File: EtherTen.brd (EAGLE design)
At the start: 68.6 x 53.3 mm, 103 parts, among them IC1 MC33269DT-5.0, IC2 APX811-44UG-7, IC3 ATMEGA16U2-MU, IC4 LM358D, IC5 ATMEGA328P TQFP32, IC6 W5100SQFP80, IC7 MCP24AA025E48, J1 DC_2_1MM, P1 USB-6PSMT, P2 ICSP:MAIN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

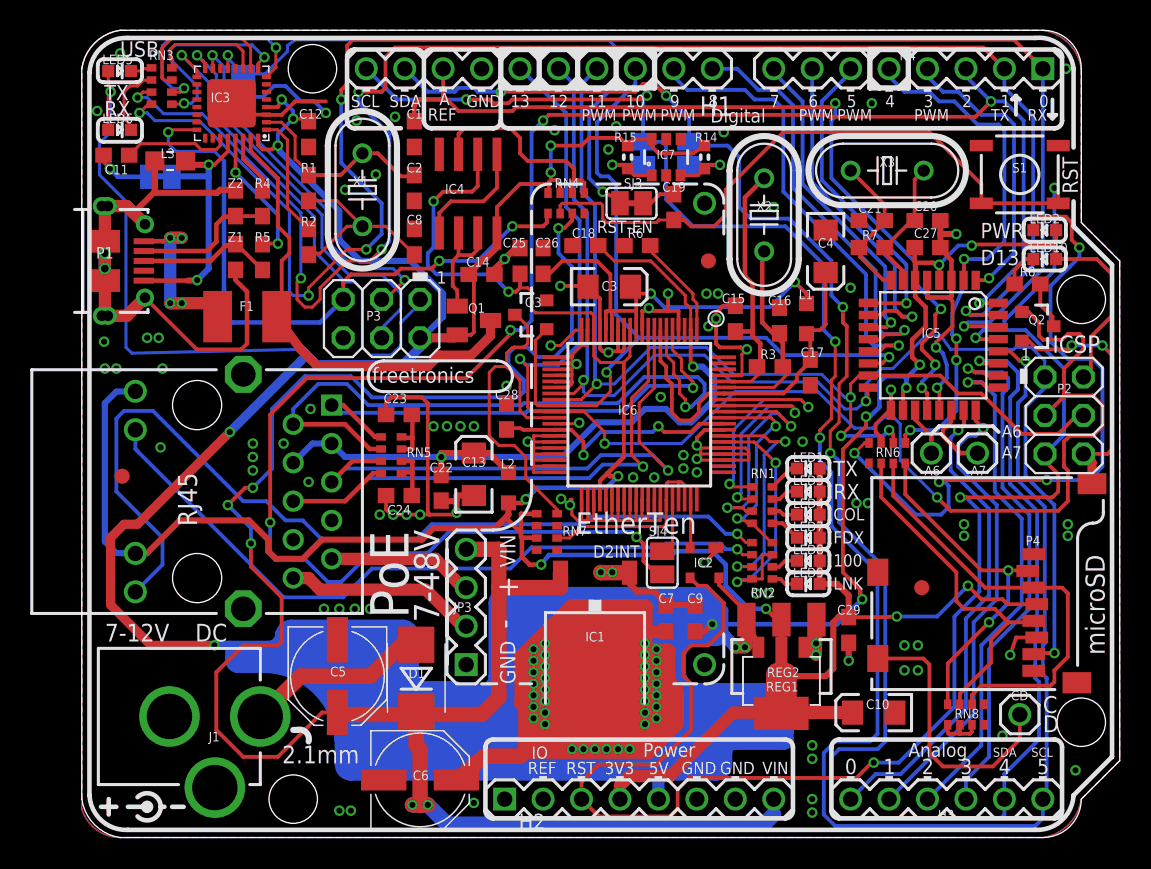
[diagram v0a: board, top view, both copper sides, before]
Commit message: Replaced most parts using SuperHouse library to add 3D models
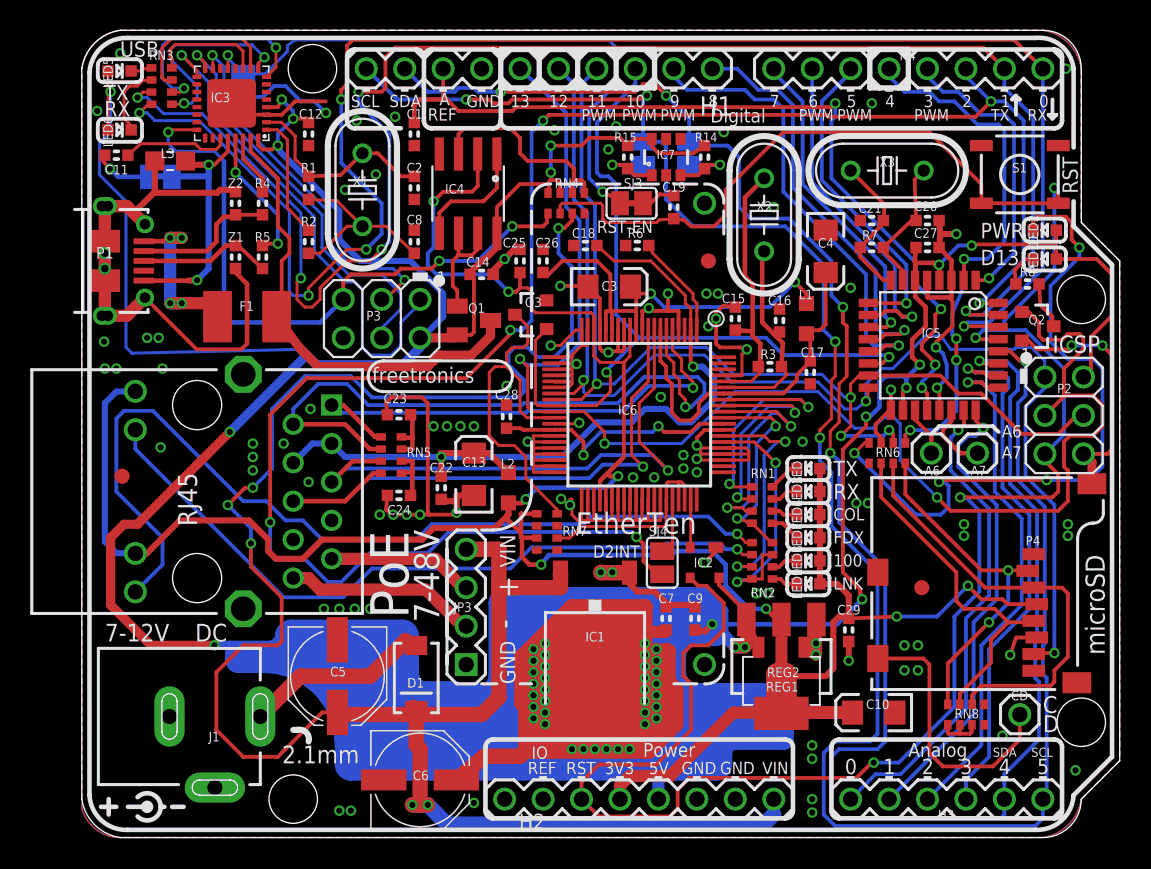
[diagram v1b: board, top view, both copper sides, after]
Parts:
- C1, C11, C12, C14, C15, C16, C17, C18, C19, C2, C20, C21, C22, C23, C24, C25, C26, C27, C28, C29, C7, C8, C9: device freetronics:0603 -> SuperHouse-DiscreteSemi:C0603
- C10, C13, C3, C4: device freetronics:EIA3216 -> SuperHouse-DiscreteSemi:EIA3216
- D1: device freetronics:SMB-DIODE -> SuperHouse-DiscreteSemi:SMA-DIODE
- F1: device rcl:L1812 -> SuperHouse-Fuses:1812
- H1: device freetronics-original:1X10 -> SuperHouse-Connectors:1X10-S
- H2: device freetronics-master-v1:1X08 -> SuperHouse-Connectors:1X08-S
- H3: device freetronics:1X06 -> SuperHouse-Connectors:1X06-S
- H4: device freetronics:1X08 -> SuperHouse-Connectors:1X08-S
- IC2: device freetronics-master-v1:SOT143-R -> SuperHouse-ICs:SOT143-R
- IC3: device freetronics-jon:ATMEL_QFN32 -> SuperHouse-MCUs:ATMEL_QFN32
- IC4: device linear:SO08 -> SuperHouse-ICs:SO08
- IC5: device freetronics-2:TQFP32-08 -> SuperHouse-MCUs:TQFP32-08
- IC6: device freetronics-marc:SQFP80 -> SuperHouse-ICs:SQFP80
- J1: device freetronics:POWER_JACK_PTH -> SuperHouse-Connectors:POWER_JACK_SLOTS
- L3: device freetronics-master-v1:0805-LARGE -> SuperHouse-DiscreteSemi:0805-LARGE
- LED1, LED10, LED2, LED3, LED4, LED5, LED6, LED7, LED8, LED9: device freetronics:LED-0603 -> SuperHouse-LEDs:LED-0603
- P1: value USB-6PSMT -> USB-6P-SMT; device freetronics-jon:USB-MICROB-MB05PMXX -> SuperHouse-Connectors:USB-MICROB-MB05PMXX
- P2, P3: device pinhead:2X03 -> SuperHouse-Connectors:2X03PTH
- P4: device freetronics-master-v1:MICRO-SD-SOCKET-PP -> SuperHouse-Connectors:MICRO-SD-SOCKET-PP
- Q3: device freetronics:SOT23-3 -> SuperHouse-DiscreteSemi:SOT23-3
- R1, R2, R3, R4, R5, R6, R7, R8: device freetronics:0603 -> SuperHouse-DiscreteSemi:R0603
- R14, R15: device freetronics-master-v1.1:0603 -> SuperHouse-DiscreteSemi:R0603
- RN1, RN2, RN3, RN4, RN5, RN6, RN7, RN8: device freetronics-master-v1:CAY16 -> SuperHouse-DiscreteSemi:CAY16
- S1: device freetronics:TACTILE_SWITCH_SMD -> SuperHouse-Switches:TACTILE_SMD-6MM
- SJ5, SJ6: value (none) -> SJCN
- U1: device freetronics-jon:HY931147C -> SuperHouse-Connectors:HY931147C
- X1, X2, X3: device freetronics-master-v1:HC49U-V -> SuperHouse-Oscillators:HC49U-V
- Z1, Z2: device freetronics:0603 -> SuperHouse-DiscreteSemi:TVS0603
- turned D1 to 270 degrees
- turned LED1 to 180 degrees
- turned LED10 to 180 degrees
- turned LED2 to 180 degrees
- turned LED3 to 180 degrees
- turned LED4 to 180 degrees
- turned LED5 to 0 degrees
- turned LED6 to 0 degrees
- turned LED7 to 180 degrees
- turned LED8 to 180 degrees
- turned LED9 to 180 degrees

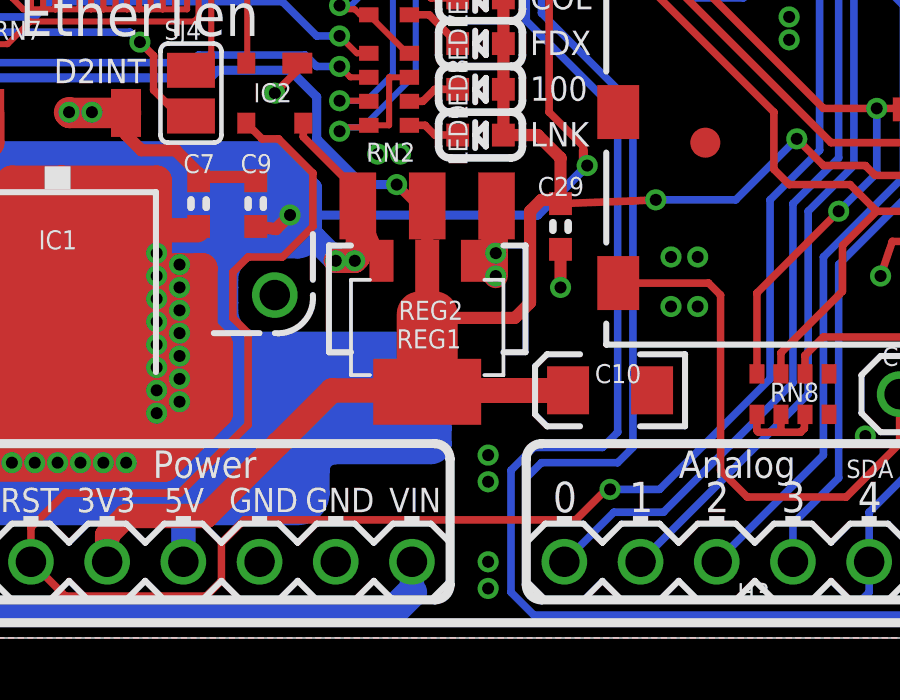
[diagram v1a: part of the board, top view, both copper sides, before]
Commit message: Replaced more parts using SuperHouse libraries
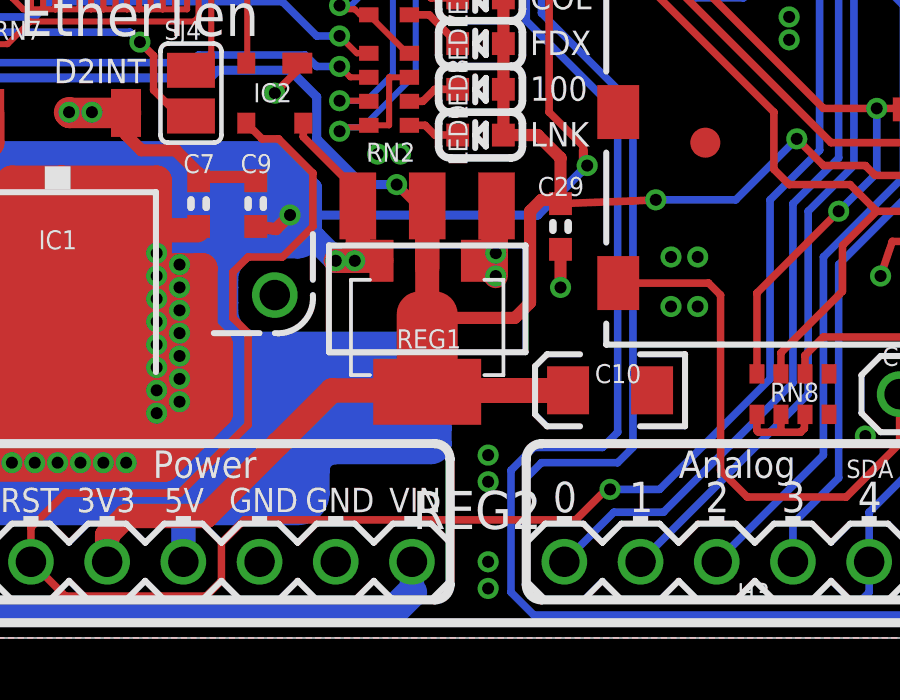
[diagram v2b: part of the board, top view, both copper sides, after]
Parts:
- Q2: device freetronics:SOT23-3 -> SuperHouse-DiscreteSemi:SOT23-3
- REG2: value LD1117-SOT223 -> LD1117; device freetronics:SOT223 -> SuperHouse-Regulators:SOT-223
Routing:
- net 5V: track 1240.7 -> 1239.6 mm
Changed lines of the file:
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@@
 </layers>
 <board>
-<fusionsync huburn="a.cGVyc29uYWw6dWUyZDliZmNi" projecturn="a.cGVyc29uYWw6dWUyZDliZmNiIzIwMTkwNjI3MjAxMDc2Mjgx" f3durn="urn:adsk.wipprod:dm.lineage:dv_ktKm1TSqk5Z0KOC4rwg" pcbguid="f52a2f92-cc1b-4903-aee4-988a1a1d0488" lastpulledtime="" lastsyncedchangeguid="7c4ccc41-8318-d7eb-12fa-0676a58a8a01"/>
+<fusionsync huburn="a.cGVyc29uYWw6dWUyZDliZmNi" projecturn="a.cGVyc29uYWw6dWUyZDliZmNiIzIwMTkwNjI3MjAxMDc2Mjgx" f3durn="urn:adsk.wipprod:dm.lineage:dv_ktKm1TSqk5Z0KOC4rwg" pcbguid="f52a2f92-cc1b-4903-aee4-988a1a1d0488" lastpulledtime="" lastsyncedchangeguid="42844e33-5a07-b25f-797f-d099163c2932"/>
 <plain>
 <wire x1="0" y1="2.54" x2="2.54" y2="0" width="0" layer="20" curve="73.740878"/>
@@
 <element name="FID1" library="freetronics" package="FIDUCIAL-1X2.5" value="FIDUCIAL1X2.5" x="41.402" y="38.1" smashed="yes"/>
 <element name="FID2" library="freetronics" package="FIDUCIAL-1X2.5" value="FIDUCIAL1X2.5" x="55.499" y="16.51" smashed="yes"/>
-<element name="REG2" library="freetronics" package="SOT223" value="LD1117-SOT223" x="46.228" y="11.303" smashed="yes" rot="R180">
-<attribute name="NAME" x="45.2755" y="10.6045" size="0.635" layer="25" ratio="17"/>
-<attribute name="VALUE" x="47.3075" y="11.4935" size="0.635" layer="27" ratio="17" rot="R180"/>
-</element>
 <element name="REG1" library="freetronics" package="SOT89" value="LD1117-SOT89" x="46.228" y="10.668" smashed="yes" rot="R180">
 <attribute name="NAME" x="45.212" y="9.652" size="0.635" layer="25" ratio="17"/>
@@
 <attribute name="VALUE" x="54.864" y="37.846" size="0.635" layer="27" font="vector" ratio="17"/>
 </element>
-<element name="Q2" library="freetronics" package="SOT23-3" value="2N7002" x="63.119" y="33.782" smashed="yes" rot="R270">
+<element name="Q2" library="SuperHouse-DiscreteSemi" library_urn="urn:adsk.eagle:library:11768461" package="SOT23-3" package3d_urn="urn:adsk.eagle:package:11815952/3" value="2N7002" x="63.119" y="33.782" smashed="yes" rot="R270">
 <attribute name="NAME" x="62.5475" y="33.909" size="0.635" layer="25" ratio="17"/>
 <attribute name="VALUE" x="62.9285" y="34.798" size="0.635" layer="27" ratio="17" rot="R270"/>
@@
 <attribute name="VALUE" x="37.084" y="44.8119" size="0.02" layer="28" rot="MR270"/>
 </element>
+<element name="REG2" library="SuperHouse-Regulators" library_urn="urn:adsk.eagle:library:11786698" package="SOT-223" package3d_urn="urn:adsk.eagle:package:11860990/2" value="LD1117" x="46.228" y="11.303" smashed="yes" rot="R180">
+<attribute name="NAME" x="50.038" y="4.9022" size="1.27" layer="25" rot="R180"/>
+<attribute name="VALUE" x="50.038" y="6.2738" size="1.27" layer="27" rot="R180"/>
+</element>
 </elements>
 <signals>
@@
 <contactref element="C24" pad="2"/>
 <contactref element="C23" pad="2"/>
-<contactref element="REG2" pad="1"/>
 <contactref element="C15" pad="2"/>
 <contactref element="C16" pad="2"/>
@@
 <wire x1="47.752" y1="12.827" x2="48.514" y2="13.589" width="0.254" layer="1"/>
 <wire x1="48.514" y1="13.589" x2="48.514" y2="14.3764" width="0.254" layer="1"/>
-<wire x1="48.514" y1="14.3764" x2="48.5394" y2="14.4018" width="0.254" layer="1"/>
 <wire x1="57.22" y1="6.915" x2="57.22" y2="7.453" width="0.254" layer="1"/>
 <wire x1="57.277" y1="6.858" x2="57.22" y2="6.915" width="0.254" layer="1"/>
@@
 <via x="45.72" y="41.656" extent="1-16" drill="0.4"/>
 <via x="34.798" y="45.466" extent="1-16" drill="0.4"/>
+<contactref element="REG2" pad="1"/>
 </signal>
 <signal name="TXOP">
@@
 <contactref element="LED3" pad="A"/>
 <contactref element="LED9" pad="A"/>
-<contactref element="REG2" pad="2"/>
-<contactref element="REG2" pad="4"/>
 <contactref element="REG1" pad="2"/>
 <contactref element="REG1" pad="4"/>
@@
 <wire x1="46.228" y1="10.668" x2="46.228" y2="9.728" width="0.4064" layer="1"/>
 <wire x1="46.228" y1="12.319" x2="46.228" y2="10.668" width="0.4064" layer="1"/>
-<wire x1="46.228" y1="14.4018" x2="46.228" y2="12.319" width="0.4064" layer="1"/>
 <wire x1="2.286" y1="18.796" x2="3.54" y2="18.775" width="0.4064" layer="16"/>
 <wire x1="1.524" y1="19.558" x2="2.286" y2="18.796" width="0.4064" layer="16"/>
@@
 <wire x1="41.275" y1="6.477" x2="38.862" y2="4.064" width="0.8128" layer="1"/>
 <wire x1="43.053" y1="8.252" x2="41.275" y2="6.477" width="0.8128" layer="1"/>
-<wire x1="50.924" y1="8.255" x2="43.053" y2="8.252" width="0.8128" layer="1"/>
+<wire x1="50.924" y1="8.255" x2="46.227953125" y2="8.253209375" width="0.8128" layer="1"/>
+<wire x1="46.227953125" y1="8.253209375" x2="43.053" y2="8.252" width="0.8128" layer="1"/>
 <wire x1="46.177" y1="8.255" x2="50.924" y2="8.255" width="0.8128" layer="1"/>
-<wire x1="46.228" y1="8.204" x2="46.177" y2="8.255" width="0.8128" layer="1"/>
-<wire x1="46.228" y1="9.728" x2="46.228" y2="8.204" width="0.3048" layer="1"/>
 <wire x1="46.228" y1="10.668" x2="49.149" y2="10.668" width="0.4064" layer="1"/>
 <wire x1="49.149" y1="10.668" x2="49.657" y2="11.176" width="0.4064" layer="1"/>
@@
 <wire x1="42.545" y1="16.637" x2="44.069" y2="15.113" width="0.3048" layer="16"/>
 <wire x1="44.069" y1="15.113" x2="45.212" y2="15.113" width="0.3048" layer="16"/>
-<wire x1="45.212" y1="15.113" x2="45.974" y2="14.351" width="0.3048" layer="1"/>
-<wire x1="45.974" y1="14.351" x2="46.228" y2="14.4018" width="0.3048" layer="1"/>
+<wire x1="45.974" y1="14.351" x2="45.212" y2="15.113" width="0.3048" layer="1"/>
 <via x="58.547" y="16.637" extent="1-16" drill="0.4"/>
 <via x="53.848" y="14.605" extent="1-16" drill="0.4"/>
@@
 <contactref element="H2" pad="4"/>
 <wire x1="35.56" y1="3.429" x2="35.56" y2="2.54" width="0.8128" layer="1"/>
+<contactref element="REG2" pad="4"/>
+<contactref element="REG2" pad="2"/>
+<wire x1="46.228" y1="9.728" x2="46.228" y2="8.204" width="0.8128" layer="1"/>
+<wire x1="46.228" y1="12.319" x2="46.228" y2="14.4018" width="0.8128" layer="1"/>
+<wire x1="46.228" y1="14.4018" x2="46.0248" y2="14.4018" width="0.4064" layer="1"/>
+<wire x1="46.0248" y1="14.4018" x2="45.974" y2="14.351" width="0.4064" layer="1"/>
+<wire x1="46.228" y1="8.204" x2="46.227953125" y2="8.204046875" width="0.4064" layer="1"/>
+<wire x1="46.227953125" y1="8.204046875" x2="46.227953125" y2="8.253209375" width="0.4064" layer="1"/>
 </signal>
 <signal name="N$1">
@@
 </signal>
 <signal name="5V" class="1">
-<contactref element="REG2" pad="3"/>
 <contactref element="REG1" pad="3"/>
 <contactref element="C27" pad="1"/>
@@
 <contactref element="RN4" pad="7"/>
 <contactref element="RN4" pad="8"/>
-<wire x1="43.9166" y1="14.4018" x2="44.704" y2="12.573" width="0.4064" layer="1"/>
 <wire x1="1.745" y1="49.276" x2="1.733" y2="50.651" width="0.2032" layer="1"/>
 <wire x1="12.21" y1="48.26" x2="12.206" y2="48.264" width="0.254" layer="1"/>
@@
 <wire x1="30.607" y1="12.827" x2="30.861" y2="12.827" width="0.8128" layer="1"/>
 <wire x1="37.211" y1="12.827" x2="37.211" y2="13.716" width="0.8128" layer="16"/>
-<wire x1="43.9166" y1="12.6746" x2="43.9166" y2="14.4018" width="0.8128" layer="1"/>
-<wire x1="43.815" y1="12.573" x2="43.9166" y2="12.6746" width="0.8128" layer="1"/>
-<wire x1="43.815" y1="12.573" x2="43.18" y2="12.573" width="0.8128" layer="1"/>
+<wire x1="43.18" y1="12.573" x2="43.815" y2="12.573" width="0.8128" layer="1"/>
 <wire x1="43.219" y1="12.573" x2="43.815" y2="12.573" width="0.8128" layer="16"/>
 <wire x1="43.219" y1="12.573" x2="43.18" y2="12.573" width="0.8128" layer="16"/>
@@
 <wire x1="42.164" y1="13.628" x2="37.885" y2="13.628" width="0.8128" layer="16"/>
 <wire x1="37.885" y1="13.628" x2="37.211" y2="12.827" width="0.8128" layer="16"/>
-<wire x1="43.9166" y1="14.4018" x2="43.9166" y2="14.8844" width="0.254" layer="1"/>
 <wire x1="43.9166" y1="14.8844" x2="42.098" y2="16.703" width="0.254" layer="1"/>
 <wire x1="42.098" y1="16.703" x2="42.098" y2="17.161" width="0.254" layer="1"/>
@@
 <wire x1="29.972" y1="9.398" x2="29.972" y2="9.144" width="1.016" layer="1"/>
 <wire x1="29.845" y1="9.398" x2="29.972" y2="9.398" width="1.016" layer="1"/>
+<contactref element="REG2" pad="3"/>
+<wire x1="43.815" y1="12.573" x2="44.704" y2="12.573" width="0.8128" layer="1"/>
+<wire x1="43.815" y1="12.573" x2="43.9166" y2="12.6746" width="0.8128" layer="1"/>
+<wire x1="43.9166" y1="12.6746" x2="43.9166" y2="14.4018" width="0.8128" layer="1"/>
+<wire x1="43.9166" y1="14.4018" x2="43.9166" y2="14.8844" width="0.4064" layer="1"/>
 </signal>
 <signal name="1V8_OUT">
